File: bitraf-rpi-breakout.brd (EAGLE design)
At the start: 66.7 x 48.9 mm, 20 parts, among them IC1 74HC595N, K1 FTR-F3FTR-F3AA005E, T1 BC547

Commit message: o Changing LED resistors from 330 to 820 ohm.
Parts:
- R1, R2, R3, R4: value 330 -> 820
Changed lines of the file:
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@@
 <element name="IC1" library="74xx-eu" package="DIL16" value="74HC595N" x="21.2725" y="37.465" rot="R90"/>
 <element name="T1" library="transistor" package="TO92" value="BC547" x="23.8125" y="14.605" rot="R180"/>
-<element name="R1" library="resistor" package="0204/7" value="330" x="39.0525" y="40.005"/>
-<element name="R2" library="resistor" package="0204/7" value="330" x="39.0525" y="46.355"/>
-<element name="R3" library="eagle-ltspice" package="R1206" value="330" x="39.0525" y="32.385" rot="MR180">
+<element name="R1" library="resistor" package="0204/7" value="820" x="39.0525" y="40.005"/>
+<element name="R2" library="resistor" package="0204/7" value="820" x="39.0525" y="46.355"/>
+<element name="R3" library="eagle-ltspice" package="R1206" value="820" x="39.0525" y="32.385" rot="MR180">
 <attribute name="SPICEMODEL" value="NONE" x="39.0525" y="32.385" size="1.778" layer="28" rot="MR180" display="off"/>
 <attribute name="SPICEPREFIX" value="R" x="39.0525" y="32.385" size="1.778" layer="28" rot="MR180" display="off"/>
 </element>
-<element name="R4" library="eagle-ltspice" package="R1206" value="330" x="39.0525" y="34.925" rot="MR180">
+<element name="R4" library="eagle-ltspice" package="R1206" value="820" x="39.0525" y="34.925" rot="MR180">
 <attribute name="SPICEMODEL" value="NONE" x="39.0525" y="34.925" size="1.778" layer="28" rot="MR180" display="off"/>
 <attribute name="SPICEPREFIX" value="R" x="39.0525" y="34.925" size="1.778" layer="28" rot="MR180" display="off"/>

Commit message: Nits
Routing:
- net VCC: track 184.6 -> 190.2 mm
- net GND: track 199.7 -> 202.7 mm

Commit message: o Rev D.
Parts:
- added R8, R9: 3.3k, resistor:0204/7
- R6, R7: value 4.7k -> 3.3k
- moved R5 7.11 mm to (37.3, 24.1)
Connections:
- new net N$11: D1.C, R7.2, R9.2
- new net N$18: D2.C, R6.2, R8.2
- net N$8: now also R8.1; no longer D2.C, R6.2
- net N$9: now also R9.1; no longer D1.C, R7.2
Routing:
- net N$9: track 56.2 -> 21.6 mm
- net N$8: track 64.8 -> 32.0 mm
- net N$18: track 0.00 -> 27.6 mm
- net N$11: track 0.00 -> 27.1 mm
- net N$6: track 12.3 -> 18.3 mm
- net N$7: track 8.56 -> 14.0 mm
- net VCC: track 190.2 -> 189.7 mm
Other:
- board text added: "Bitraf R-π Brk 2013 Rev D"
- board text removed: "Bitraf R-π Brk 2013 Rev B"

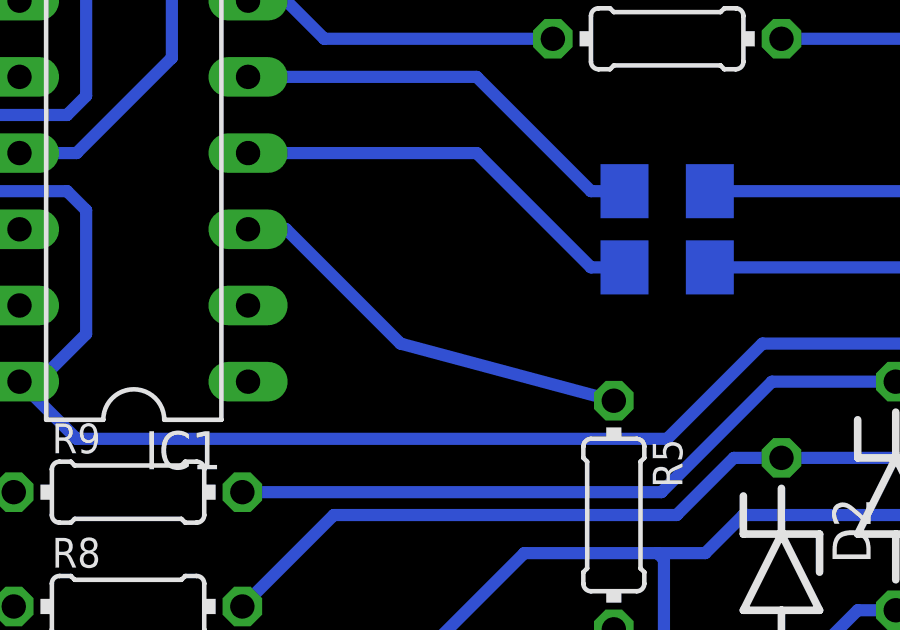
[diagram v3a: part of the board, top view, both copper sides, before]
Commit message: o Bigger pads on relay.
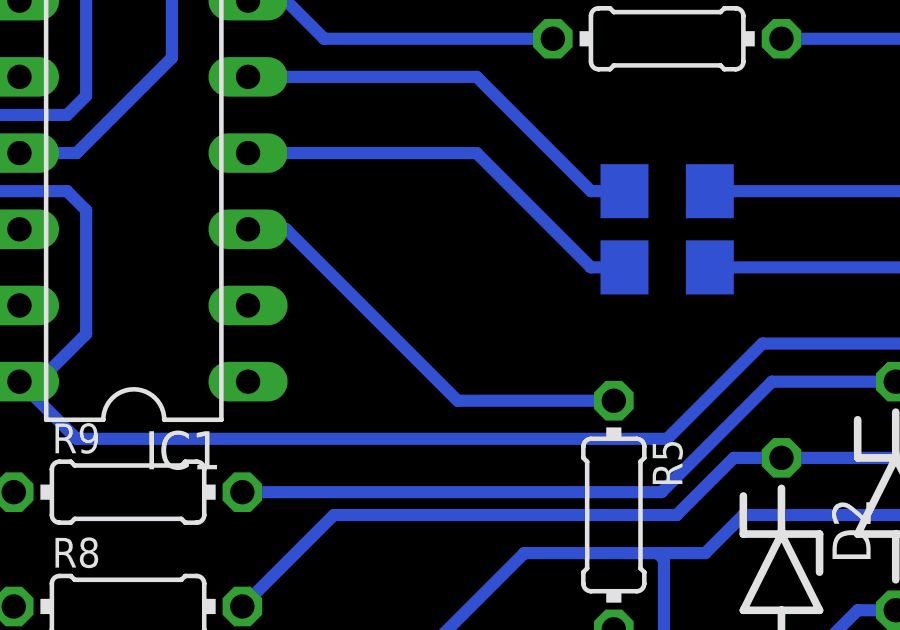
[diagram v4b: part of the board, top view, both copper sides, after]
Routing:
- net N$7: track 14.0 -> 14.6 mm
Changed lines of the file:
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@@
 <grid distance="25" unitdist="mil" unit="mil" style="lines" multiple="1" display="no" altdistance="0.000123031496" altunitdist="mil" altunit="mil"/>
 <layers>
-<layer number="1" name="Top" color="4" fill="1" visible="yes" active="yes"/>
+<layer number="1" name="Top" color="4" fill="1" visible="no" active="yes"/>
 <layer number="16" name="Bottom" color="1" fill="1" visible="yes" active="yes"/>
 <layer number="17" name="Pads" color="2" fill="1" visible="yes" active="yes"/>
 <layer number="18" name="Vias" color="2" fill="1" visible="yes" active="yes"/>
-<layer number="19" name="Unrouted" color="6" fill="1" visible="yes" active="yes"/>
-<layer number="20" name="Dimension" color="15" fill="1" visible="yes" active="yes"/>
-<layer number="21" name="tPlace" color="7" fill="1" visible="yes" active="yes"/>
-<layer number="22" name="bPlace" color="7" fill="1" visible="yes" active="yes"/>
-<layer number="23" name="tOrigins" color="15" fill="1" visible="yes" active="yes"/>
-<layer number="24" name="bOrigins" color="15" fill="1" visible="yes" active="yes"/>
-<layer number="25" name="tNames" color="7" fill="1" visible="yes" active="yes"/>
-<layer number="26" name="bNames" color="7" fill="1" visible="yes" active="yes"/>
-<layer number="27" name="tValues" color="7" fill="1" visible="yes" active="yes"/>
-<layer number="28" name="bValues" color="7" fill="1" visible="yes" active="yes"/>
+<layer number="19" name="Unrouted" color="6" fill="1" visible="no" active="yes"/>
+<layer number="20" name="Dimension" color="15" fill="1" visible="no" active="yes"/>
+<layer number="21" name="tPlace" color="7" fill="1" visible="no" active="yes"/>
+<layer number="22" name="bPlace" color="7" fill="1" visible="no" active="yes"/>
+<layer number="23" name="tOrigins" color="15" fill="1" visible="no" active="yes"/>
+<layer number="24" name="bOrigins" color="15" fill="1" visible="no" active="yes"/>
+<layer number="25" name="tNames" color="7" fill="1" visible="no" active="yes"/>
+<layer number="26" name="bNames" color="7" fill="1" visible="no" active="yes"/>
+<layer number="27" name="tValues" color="7" fill="1" visible="no" active="yes"/>
+<layer number="28" name="bValues" color="7" fill="1" visible="no" active="yes"/>
 <layer number="29" name="tStop" color="7" fill="3" visible="no" active="yes"/>
 <layer number="30" name="bStop" color="7" fill="6" visible="no" active="yes"/>
@@
 <layer number="37" name="tTest" color="7" fill="1" visible="no" active="yes"/>
 <layer number="38" name="bTest" color="7" fill="1" visible="no" active="yes"/>
-<layer number="39" name="tKeepout" color="4" fill="11" visible="yes" active="yes"/>
-<layer number="40" name="bKeepout" color="1" fill="11" visible="yes" active="yes"/>
-<layer number="41" name="tRestrict" color="4" fill="10" visible="yes" active="yes"/>
-<layer number="42" name="bRestrict" color="1" fill="10" visible="yes" active="yes"/>
-<layer number="43" name="vRestrict" color="2" fill="10" visible="yes" active="yes"/>
-<layer number="44" name="Drills" color="7" fill="1" visible="yes" active="yes"/>
-<layer number="45" name="Holes" color="7" fill="1" visible="yes" active="yes"/>
-<layer number="46" name="Milling" color="3" fill="1" visible="yes" active="yes"/>
+<layer number="39" name="tKeepout" color="4" fill="11" visible="no" active="yes"/>
+<layer number="40" name="bKeepout" color="1" fill="11" visible="no" active="yes"/>
+<layer number="41" name="tRestrict" color="4" fill="10" visible="no" active="yes"/>
+<layer number="42" name="bRestrict" color="1" fill="10" visible="no" active="yes"/>
+<layer number="43" name="vRestrict" color="2" fill="10" visible="no" active="yes"/>
+<layer number="44" name="Drills" color="7" fill="1" visible="no" active="yes"/>
+<layer number="45" name="Holes" color="7" fill="1" visible="no" active="yes"/>
+<layer number="46" name="Milling" color="3" fill="1" visible="no" active="yes"/>
 <layer number="47" name="Measures" color="7" fill="1" visible="yes" active="yes"/>
-<layer number="48" name="Document" color="7" fill="1" visible="yes" active="yes"/>
-<layer number="49" name="Reference" color="7" fill="1" visible="yes" active="yes"/>
-<layer number="51" name="tDocu" color="7" fill="1" visible="yes" active="yes"/>
-<layer number="52" name="bDocu" color="7" fill="1" visible="yes" active="yes"/>
+<layer number="48" name="Document" color="7" fill="1" visible="no" active="yes"/>
+<layer number="49" name="Reference" color="7" fill="1" visible="no" active="yes"/>
+<layer number="51" name="tDocu" color="7" fill="1" visible="no" active="yes"/>
+<layer number="52" name="bDocu" color="7" fill="1" visible="no" active="yes"/>
 <layer number="91" name="Nets" color="2" fill="1" visible="no" active="no"/>
 <layer number="92" name="Busses" color="1" fill="1" visible="no" active="no"/>
@@
 <contactref element="IC1" pad="3"/>
 <wire x1="25.0825" y1="33.655" x2="26.3525" y2="33.655" width="0.4064" layer="16"/>
-<wire x1="26.3525" y1="33.655" x2="30.1625" y2="29.845" width="0.4064" layer="16"/>
-<wire x1="30.1625" y1="29.845" x2="37.2745" y2="27.94" width="0.4064" layer="16"/>
+<wire x1="26.3525" y1="33.655" x2="32.0675" y2="27.94" width="0.4064" layer="16"/>
+<wire x1="32.0675" y1="27.94" x2="37.2745" y2="27.94" width="0.4064" layer="16"/>
 </signal>
 <signal name="N$9">
